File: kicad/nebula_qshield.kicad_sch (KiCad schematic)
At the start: 0 parts

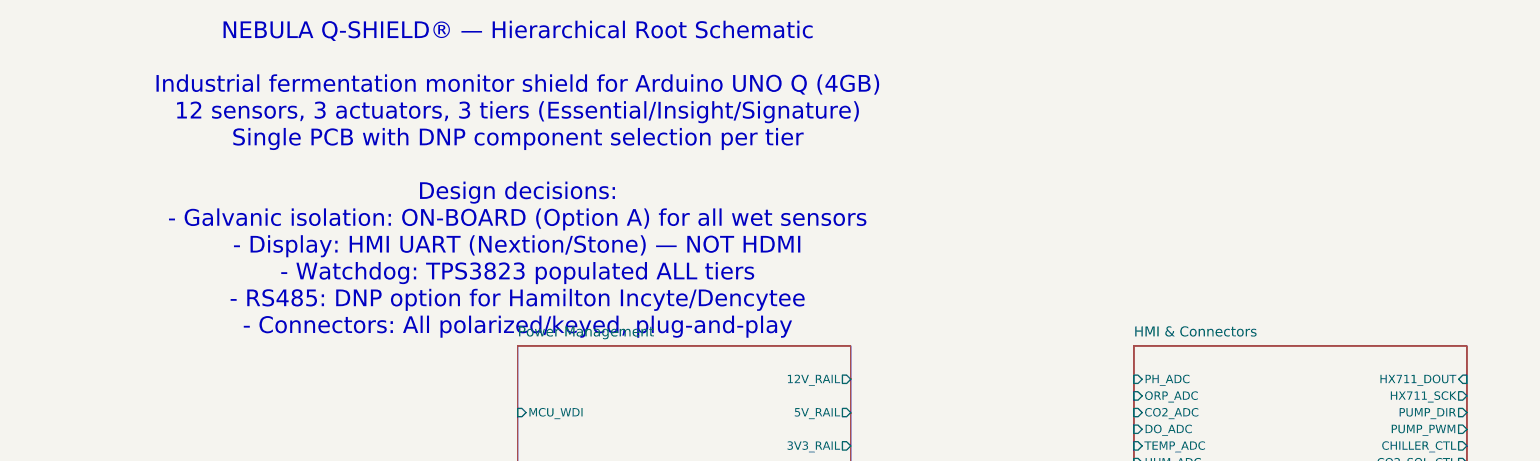
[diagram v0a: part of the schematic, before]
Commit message: fix: Embed lib_symbols, fix invalid lib_ids, bump to KiCad 9 format
- Embed complete (lib_symbols) definitions in all 5 sub-sheets so symbols
  render as real parts instead of '??' placeholders (files now self-contained)
- Substitute invalid lib_ids with valid library symbols:
  Device:CP -> Device:C_Polarized, Diode:PESD3V3S2USF -> Diode:PESD3V3S1UL,
  Diode:PESD5V0S1BSF -> Diode:PESD5V0S1UL, Isolator:PC817X2 -> Isolator:PC817
- Bump file format version 20231120 -> 20250114 (removes 'older version' warning)
- Left-justify header text blocks so long lines stay within the A3 frame

Validated: kicad-cli SVG render (all real symbols, within frame), clean-room
eeschema GUI render with broken library table (no '??'), and kicad-cli ERC
runs without crashing (425 violations are expected unconnected-pin/dangling-
label items, resolved during per-sheet wiring).

Co-Authored-By: Devin AI <158243242+devin-ai-integration[bot]@users.noreply.github.com>
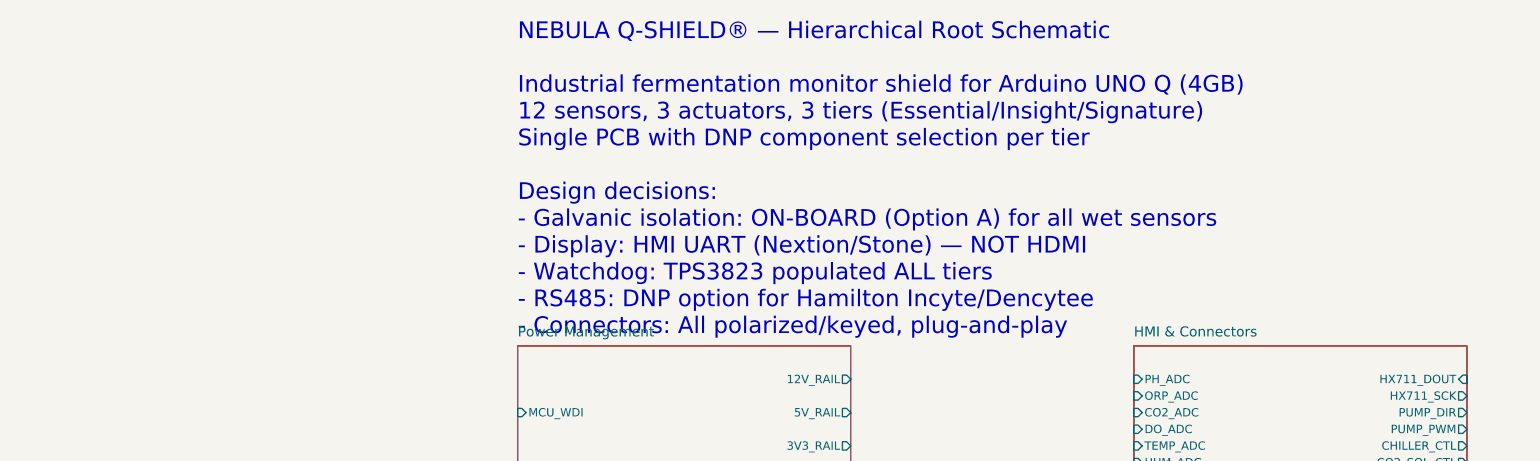
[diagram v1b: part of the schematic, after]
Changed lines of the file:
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@@
 (kicad_sch
-  (version 20231120)
+  (version 20250114)
   (generator "devin")
   (generator_version "1.0")
@@
   (text "NEBULA Q-SHIELD® — Hierarchical Root Schematic\n\nIndustrial fermentation monitor shield for Arduino UNO Q (4GB)\n12 sensors, 3 actuators, 3 tiers (Essential/Insight/Signature)\nSingle PCB with DNP component selection per tier\n\nDesign decisions:\n- Galvanic isolation: ON-BOARD (Option A) for all wet sensors\n- Display: HMI UART (Nextion/Stone) — NOT HDMI\n- Watchdog: TPS3823 populated ALL tiers\n- RS485: DNP option for Hamilton Incyte/Dencytee\n- Connectors: All polarized/keyed, plug-and-play"
     (at 25.4 25.4 0)
-    (effects (font (size 2.54 2.54)))
+    (effects (font (size 2.54 2.54)) (justify left))
   )
 )
